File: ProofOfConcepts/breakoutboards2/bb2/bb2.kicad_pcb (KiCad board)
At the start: 2 copper layers, 11 parts, among them J1 Conn_01x03_Female, U1 PAM2305CGFADJ

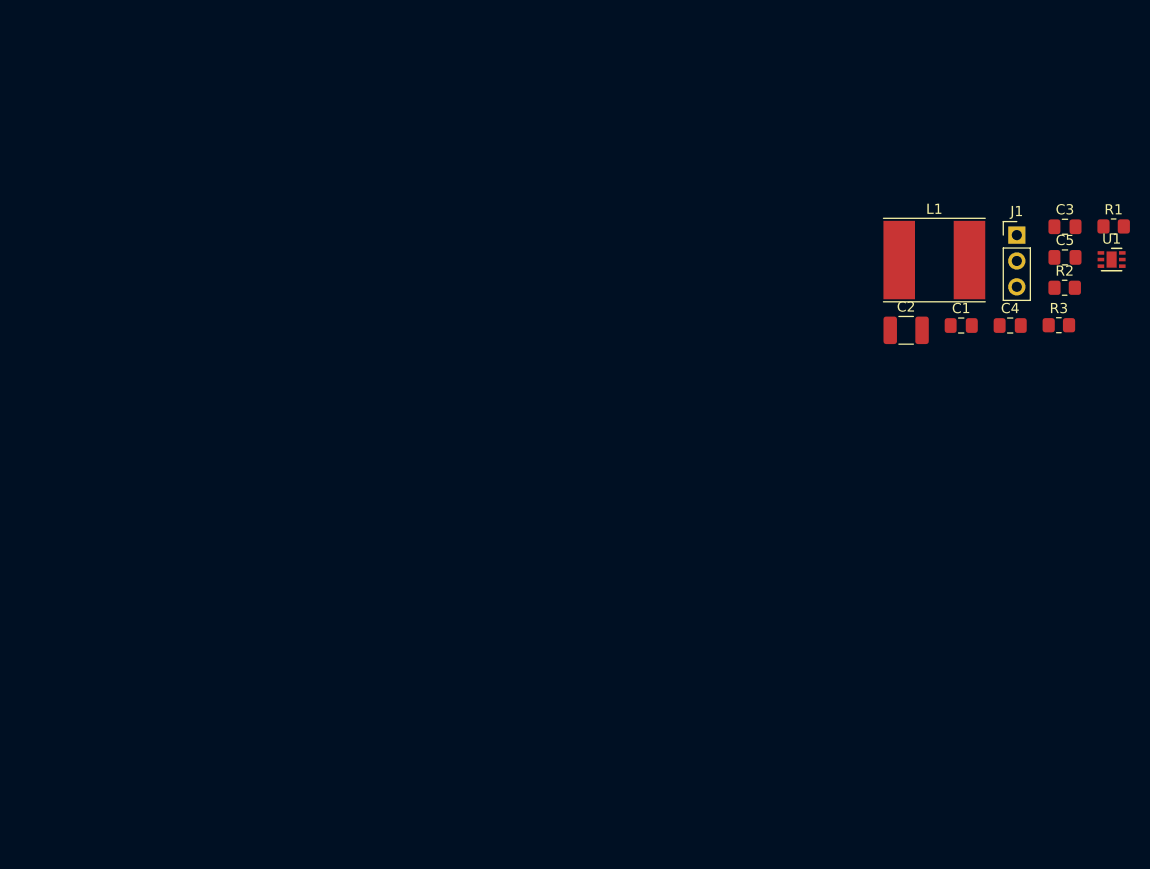
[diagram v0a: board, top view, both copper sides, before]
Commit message: breakout board for v2 buck and nmos driver
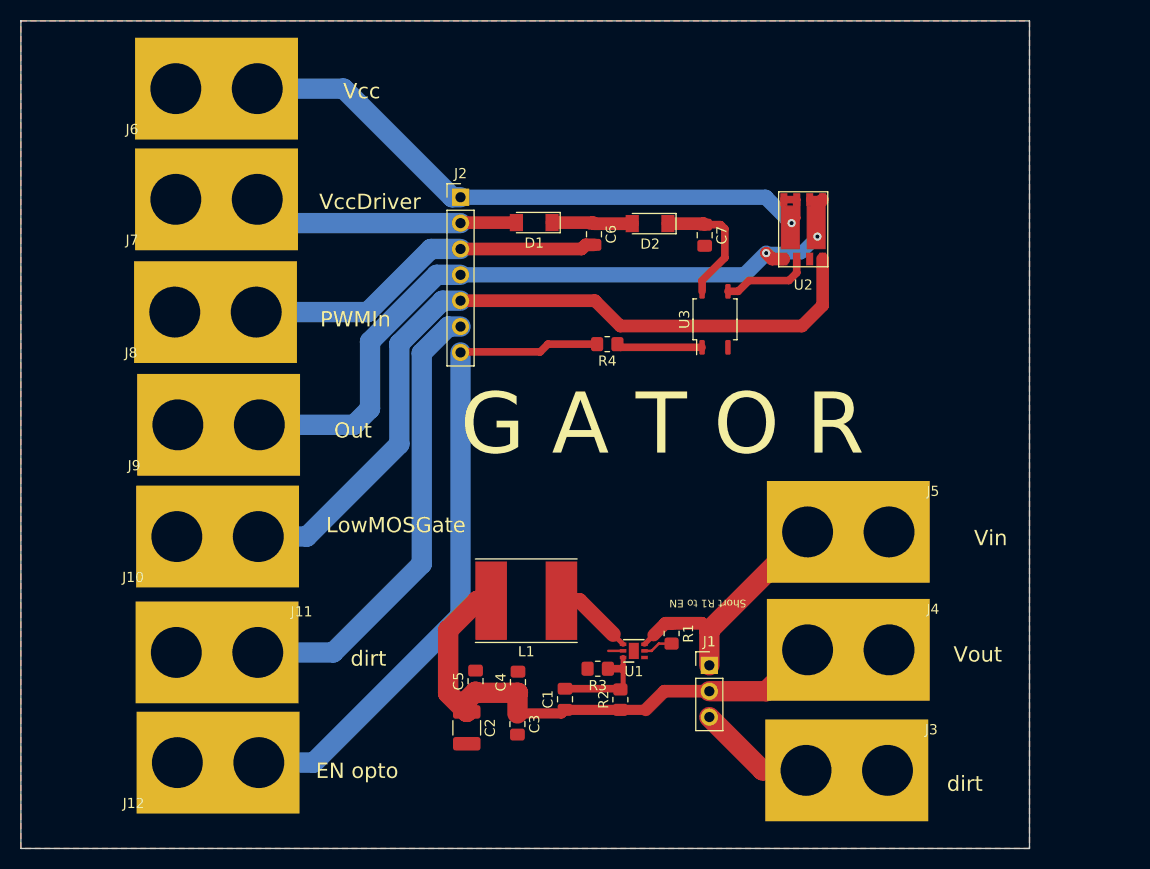
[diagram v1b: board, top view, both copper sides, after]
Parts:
- added C6: 10uF, Capacitor_SMD:C_0805_2012Metric_Pad1.18x1.45mm_HandSolder, F.Cu at (129.9, 101.0)
- added C7: 10uF, Capacitor_SMD:C_0805_2012Metric_Pad1.18x1.45mm_HandSolder, F.Cu at (140.8, 101.1)
- added D1: LL4148, Diode_SMD:D_MiniMELF, F.Cu at (124.1, 99.8)
- added D2: LL4148, Diode_SMD:D_MiniMELF, F.Cu at (135.5, 99.9)
- added J10: Conn_01x01_Male, 1KicadLib:GatorTestpoint, F.Cu at (84.5, 129.4)
- added J11: Conn_01x01_Male, 1KicadLib:GatorTestpoint, F.Cu at (101.4, 143.3)
- added J12: Conn_01x01_Male, 1KicadLib:GatorTestpoint, F.Cu at (84.5, 151.6)
- added J2: Conn_01x07_Male, Connector_PinHeader_2.54mm:PinHeader_1x07_P2.54mm_Vertical, F.Cu at (116.8, 97.3)
- added J3: Conn_01x01_Male, 1KicadLib:GatorTestpoint, F.Cu at (163.3, 154.9)
- added J4: Conn_01x01_Male, 1KicadLib:GatorTestpoint, F.Cu at (163.4, 143.1)
- added J5: Conn_01x01_Male, 1KicadLib:GatorTestpoint, F.Cu at (163.4, 131.5)
- added J6: Conn_01x01_Male, 1KicadLib:GatorTestpoint, F.Cu at (84.4, 85.4)
- added J7: Conn_01x01_Male, 1KicadLib:GatorTestpoint, F.Cu at (84.4, 96.2)
- added J8: Conn_01x01_Male, 1KicadLib:GatorTestpoint, F.Cu at (84.3, 107.3)
- added J9: Conn_01x01_Male, 1KicadLib:GatorTestpoint, F.Cu at (84.6, 118.4)
- added R4: 300, Resistor_SMD:R_0805_2012Metric_Pad1.20x1.40mm_HandSolder, F.Cu at (131.3, 111.8)
- added U2: BUK9K52-60E, 1KicadLib:LFPAK56D, F.Cu at (153.7, 102.0)
- added U3: PC817, Package_SO:SOP-4_3.8x4.1mm_P2.54mm, F.Cu at (141.8, 109.3)
- moved C3 72.6 mm to (122.4, 149.1), turned to 270 degrees
- moved C5 71.3 mm to (118.3, 144.9), turned to 90 degrees
- moved U1 60.7 mm to (133.9, 141.9), turned to 180 degrees
- moved C4 59.7 mm to (122.5, 145.0), turned to 90 degrees
- moved R2 59.5 mm to (132.5, 146.7), turned to 90 degrees
- moved R1 59.0 mm to (137.6, 140.2), turned to 270 degrees
- moved C2 58.2 mm to (117.4, 149.4), turned to 270 degrees
- moved R3 56.5 mm to (130.3, 143.6), turned to 180 degrees
- moved C1 53.5 mm to (127.1, 146.6), turned to 90 degrees
- moved L1 52.2 mm to (123.3, 137.0), turned to 180 degrees
- moved J1 51.9 mm to (141.3, 143.3)
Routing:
- net Net-(J10-Pad1): track 0.00 -> 85.2 mm
- net Net-(J2-Pad4): track 0.00 -> 81.4 mm, vias 0 -> 2
- net GND: track 0.00 -> 74.4 mm
- net Net-(J12-Pad1): track 0.00 -> 73.4 mm
- net Net-(J2-Pad1): track 0.00 -> 69.7 mm, vias 0 -> 1
- net Net-(C1-Pad1): track 0.00 -> 61.9 mm
- net Net-(C6-Pad2): track 0.00 -> 43.9 mm
- net Net-(J1-Pad1): track 0.00 -> 36.0 mm
- net Net-(D1-Pad2): track 0.00 -> 34.4 mm
- net Net-(C7-Pad1): track 0.00 -> 12.9 mm
- net Net-(C1-Pad2): track 0.00 -> 10.3 mm
- net Net-(U2-Pad2): track 0.00 -> 8.86 mm
- net Net-(R4-Pad1): track 0.00 -> 8.44 mm
- net Net-(C6-Pad1): track 0.00 -> 7.93 mm
- net Net-(L1-Pad1): track 0.00 -> 7.83 mm
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- added copper zone on B.Cu, net GND
- added copper zone on F.Cu, net GND
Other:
- board outline added: 99.1 x 81.3 mm
- board text added: "EN opto"
- board text added: "G A T O R"
- board text added: "LowMOSGate"
- board text added: "Out"
- board text added: "PWMIn"
- board text added: "Short R1 to EN"
- board text added: "Vcc"
- board text added: "VccDriver"
- board text added: "Vin"
- board text added: "Vout"
- board text added: "dirt"

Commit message: E
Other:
- net class Default removed
